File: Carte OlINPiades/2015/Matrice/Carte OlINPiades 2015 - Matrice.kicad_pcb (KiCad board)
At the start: 2 copper layers, 284 parts, among them U1 dsPIC33FJ128MC802, U2 LM7805, U3 LM2937-3.3

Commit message: avancé matrice
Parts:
- removed Batteries1: CONN_2, Connect:bornier2
- removed C1, C5, C6: 100nF, Capacitors_SMD:C_0805_HandSoldering
- removed C2, C7: 10uF, Capacitors_SMD:C_0805_HandSoldering
- removed C4: 330nF, Capacitors_SMD:C_0805_HandSoldering
- removed C8, C9: 0,1uF, Capacitors_SMD:C_0805_HandSoldering
- removed DEMUX1: 74HC4514, Housings_SOIC:SOIC-24_7.5x15.4mm_Pitch1.27mm
- removed Pickit1: CONN_5, Pin_Headers:Pin_Header_Straight_1x05
- removed R1: 10kOhm, Resistors_SMD:R_0805_HandSoldering
- removed R2: 470Ohm, Resistors_SMD:R_0805_HandSoldering
- removed R3: TODO, Resistors_SMD:R_0805_HandSoldering
- removed S1: CAT4016, Housings_SOIC:SOIC-24_7.5x15.4mm_Pitch1.27mm
- removed S2, S3, S4, S5, S6, S7, S8, S9: TPS2080, Housings_SOIC:SOIC-8_3.9x4.9mm_Pitch1.27mm
- removed U1: dsPIC33FJ128MC802, Housings_SOIC:SOIC-28_7.5x17.9mm_Pitch1.27mm
- removed U2: LM7805, Transistors_SMD:sot428
- removed U3: LM2937-3.3, Transistors_SMD:sot428
- removed UART1, UART2: CONN_2, Pin_Headers:Pin_Header_Straight_1x02
- added H1: PinHeader, Pin_Headers:Pin_Header_Straight_1x16, F.Cu at (118.7, 29.9)
- added H2: PinHeader, Pin_Headers:Pin_Header_Straight_1x16, F.Cu at (217.7, 120.5)
- moved D241 43.0 mm to (17.5, 192.3)
- moved D242 40.6 mm to (27.5, 192.3)
- moved D225 40.5 mm to (17.5, 182.3)
- moved D243 38.4 mm to (37.5, 192.3)
- moved D209 38.3 mm to (17.5, 172.3)
- moved D256 38.1 mm to (167.5, 192.3)
- moved D226 38.0 mm to (27.5, 182.3)
- moved D1 37.0 mm to (17.5, 42.3)
- moved D244 36.4 mm to (47.5, 192.3)
- moved D193 36.2 mm to (17.5, 162.3)
- moved D255 36.2 mm to (157.5, 192.3)
- moved D227 35.7 mm to (37.5, 182.3)
- moved D210 35.6 mm to (27.5, 172.3)
- moved D240 35.4 mm to (167.5, 182.3)
- moved D17 35.1 mm to (17.5, 52.3)
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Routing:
- net GND: track 377.5 -> 0.00 mm, vias 8 -> 0
- net +3.3V: track 188.5 -> 0.00 mm, vias 3 -> 0
- net Net-(D1-Pad2): track 148.0 -> 330.0 mm
- net +5V: track 155.1 -> 0.00 mm, vias 8 -> 0
- net RB11: track 101.4 -> 0.00 mm
- net RB10: track 95.8 -> 0.00 mm
- net RB7: track 90.8 -> 0.00 mm, vias 2 -> 0
- net RB6: track 87.1 -> 0.00 mm, vias 2 -> 0
- net RB9: track 86.4 -> 0.00 mm
- net RB8: track 82.2 -> 0.00 mm
- net RA2: track 69.2 -> 0.00 mm
- net RB3: track 67.0 -> 0.00 mm
- net RB2: track 66.5 -> 0.00 mm
- net Net-(DEMUX1-Pad16): track 64.6 -> 0.00 mm
- net Net-(DEMUX1-Pad15): track 63.6 -> 0.00 mm
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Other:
- rule trace_min: 0.2 -> 0.25

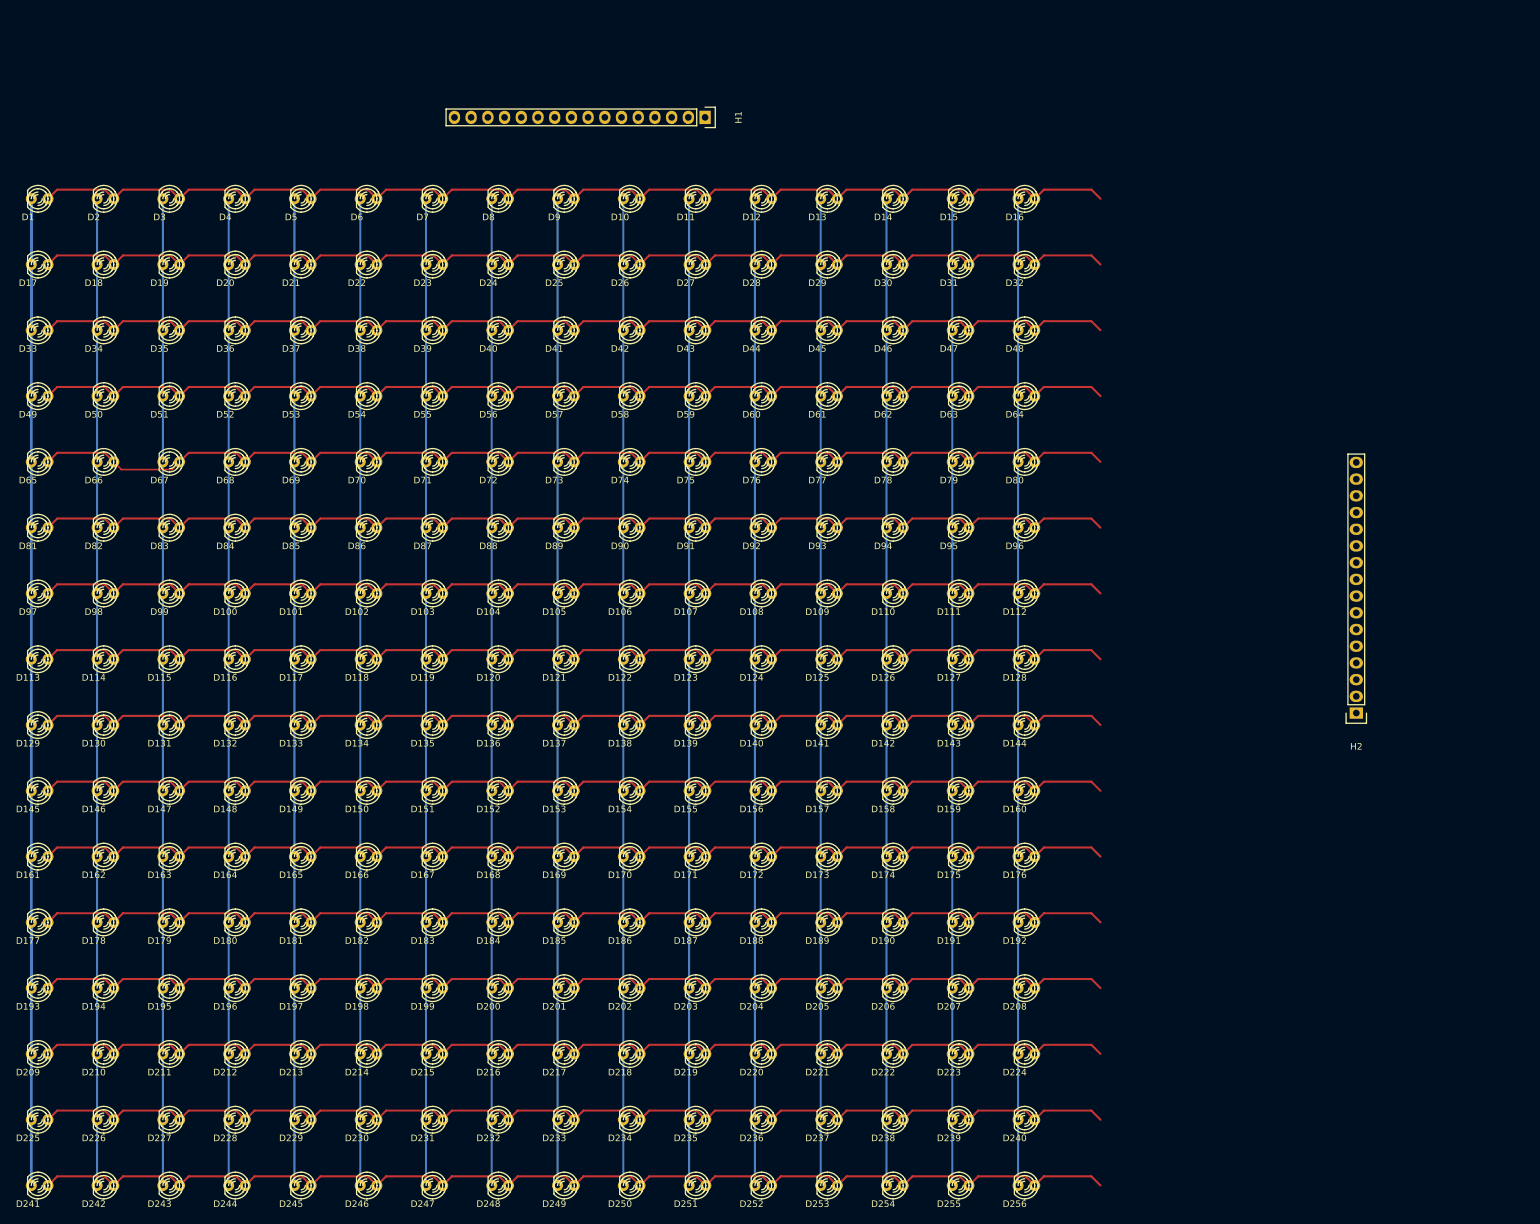
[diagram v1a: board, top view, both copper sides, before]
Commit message: fini plaque de leds
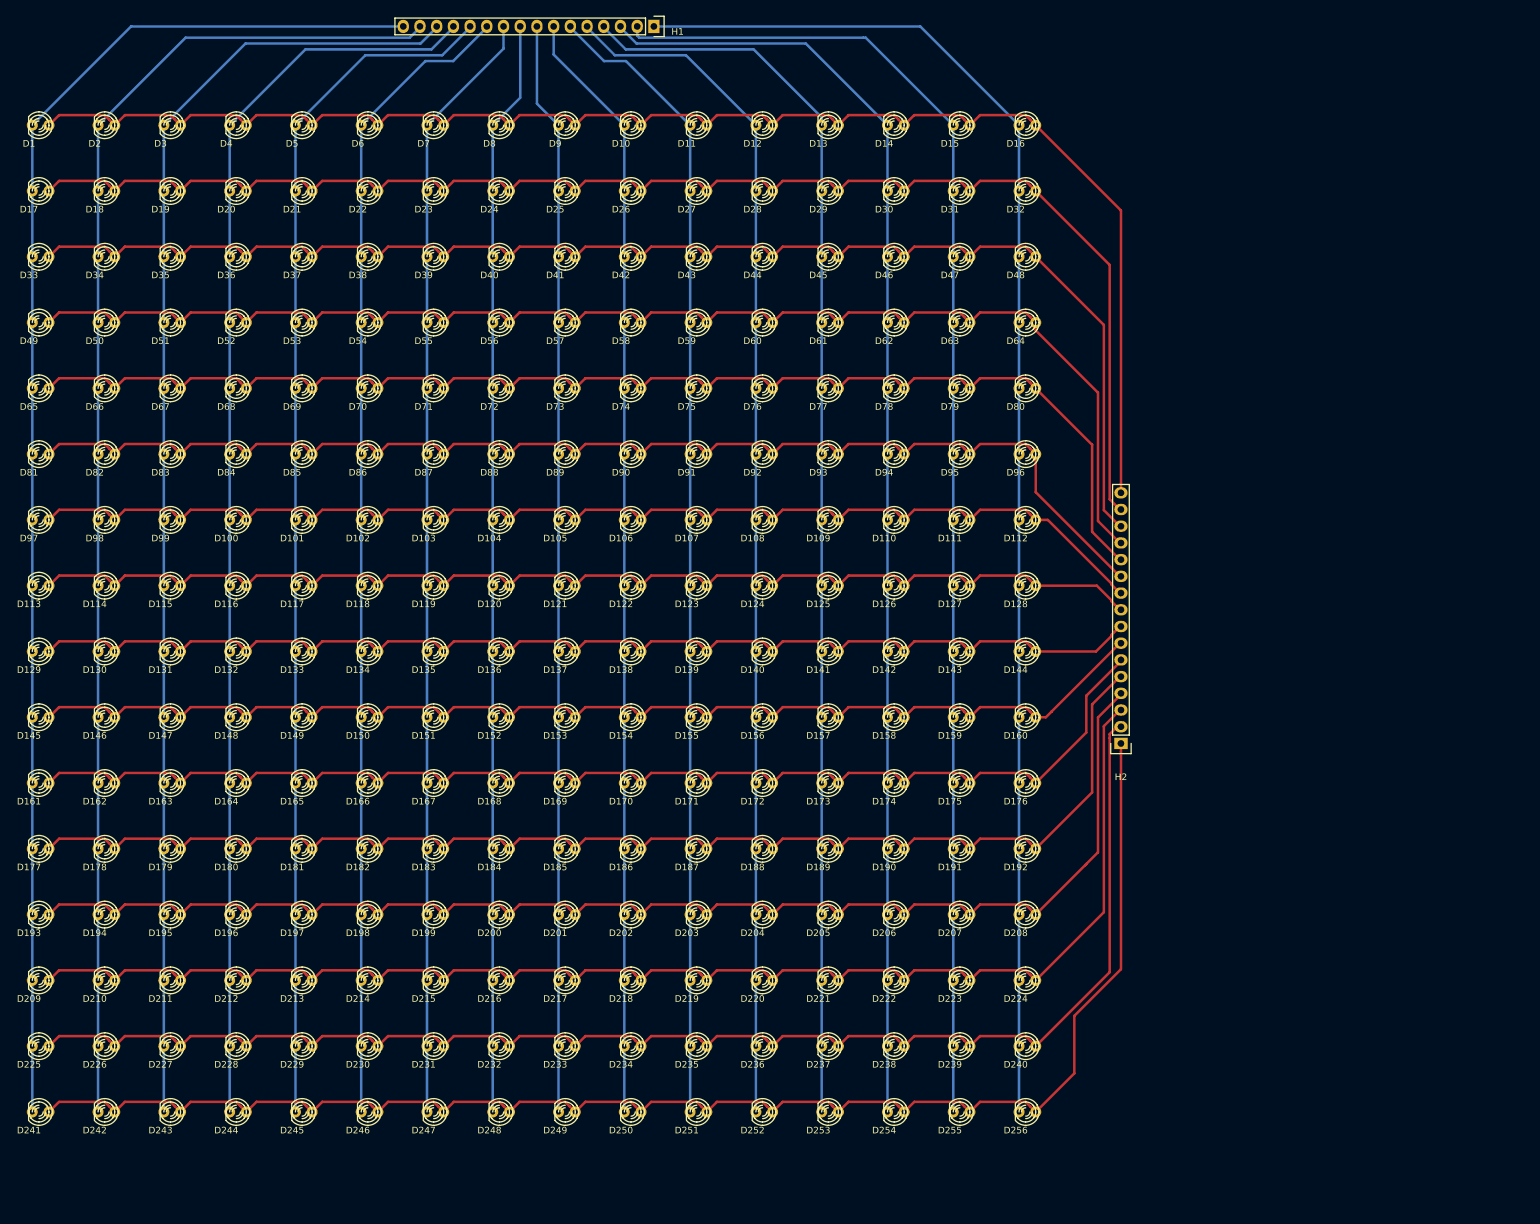
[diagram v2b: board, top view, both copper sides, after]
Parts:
- moved H2 36.1 mm to (181.9, 125.1)
- moved H1 15.9 mm to (110.9, 16.1)
- moved D1 11.2 mm to (17.7, 31.1)
- moved D10 11.2 mm to (107.7, 31.1)
- moved D100 11.2 mm to (47.7, 91.1)
- moved D101 11.2 mm to (57.7, 91.1)
- moved D102 11.2 mm to (67.7, 91.1)
- moved D103 11.2 mm to (77.7, 91.1)
- moved D104 11.2 mm to (87.7, 91.1)
- moved D105 11.2 mm to (97.7, 91.1)
- moved D106 11.2 mm to (107.7, 91.1)
- moved D107 11.2 mm to (117.7, 91.1)
- moved D108 11.2 mm to (127.7, 91.1)
- moved D109 11.2 mm to (137.7, 91.1)
- moved D11 11.2 mm to (117.7, 31.1)
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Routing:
- net Net-(D1-Pad2): track 330.0 -> 212.6 mm
- net Net-(D112-Pad2): track 150.0 -> 211.7 mm
- net Net-(D241-Pad1): track 178.5 -> 234.2 mm
- net Net-(D1-Pad1): track 178.5 -> 234.1 mm
- net Net-(D111-Pad2): track 150.0 -> 205.1 mm
- net Net-(D225-Pad1): track 178.5 -> 227.1 mm
- net Net-(D17-Pad1): track 178.5 -> 226.7 mm
- net Net-(D115-Pad2): track 150.0 -> 197.8 mm
- net Net-(D110-Pad2): track 150.0 -> 196.9 mm
- net Net-(D209-Pad1): track 178.5 -> 219.4 mm
- net Net-(D33-Pad1): track 178.5 -> 219.2 mm
- net Net-(D100-Pad2): track 150.0 -> 190.3 mm
- net Net-(D109-Pad2): track 150.0 -> 190.1 mm
- net Net-(D193-Pad1): track 178.5 -> 212.2 mm
- net Net-(D49-Pad1): track 178.5 -> 211.8 mm
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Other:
- net class Default: clearance 0.2 -> 0.4; trace_width 0.25 -> 0.308; via_dia 0.6 -> 0.8; via_drill 0.4 -> 0.6
- net class Pisa interm added: clearance 0.508, trace_width 0.381, via_dia 1, via_drill 0.8
- rule trace_clearance: 0.2 -> 0.4
- rule trace_min: 0.25 -> 0.308

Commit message: retourné matrice, exporté pdfs
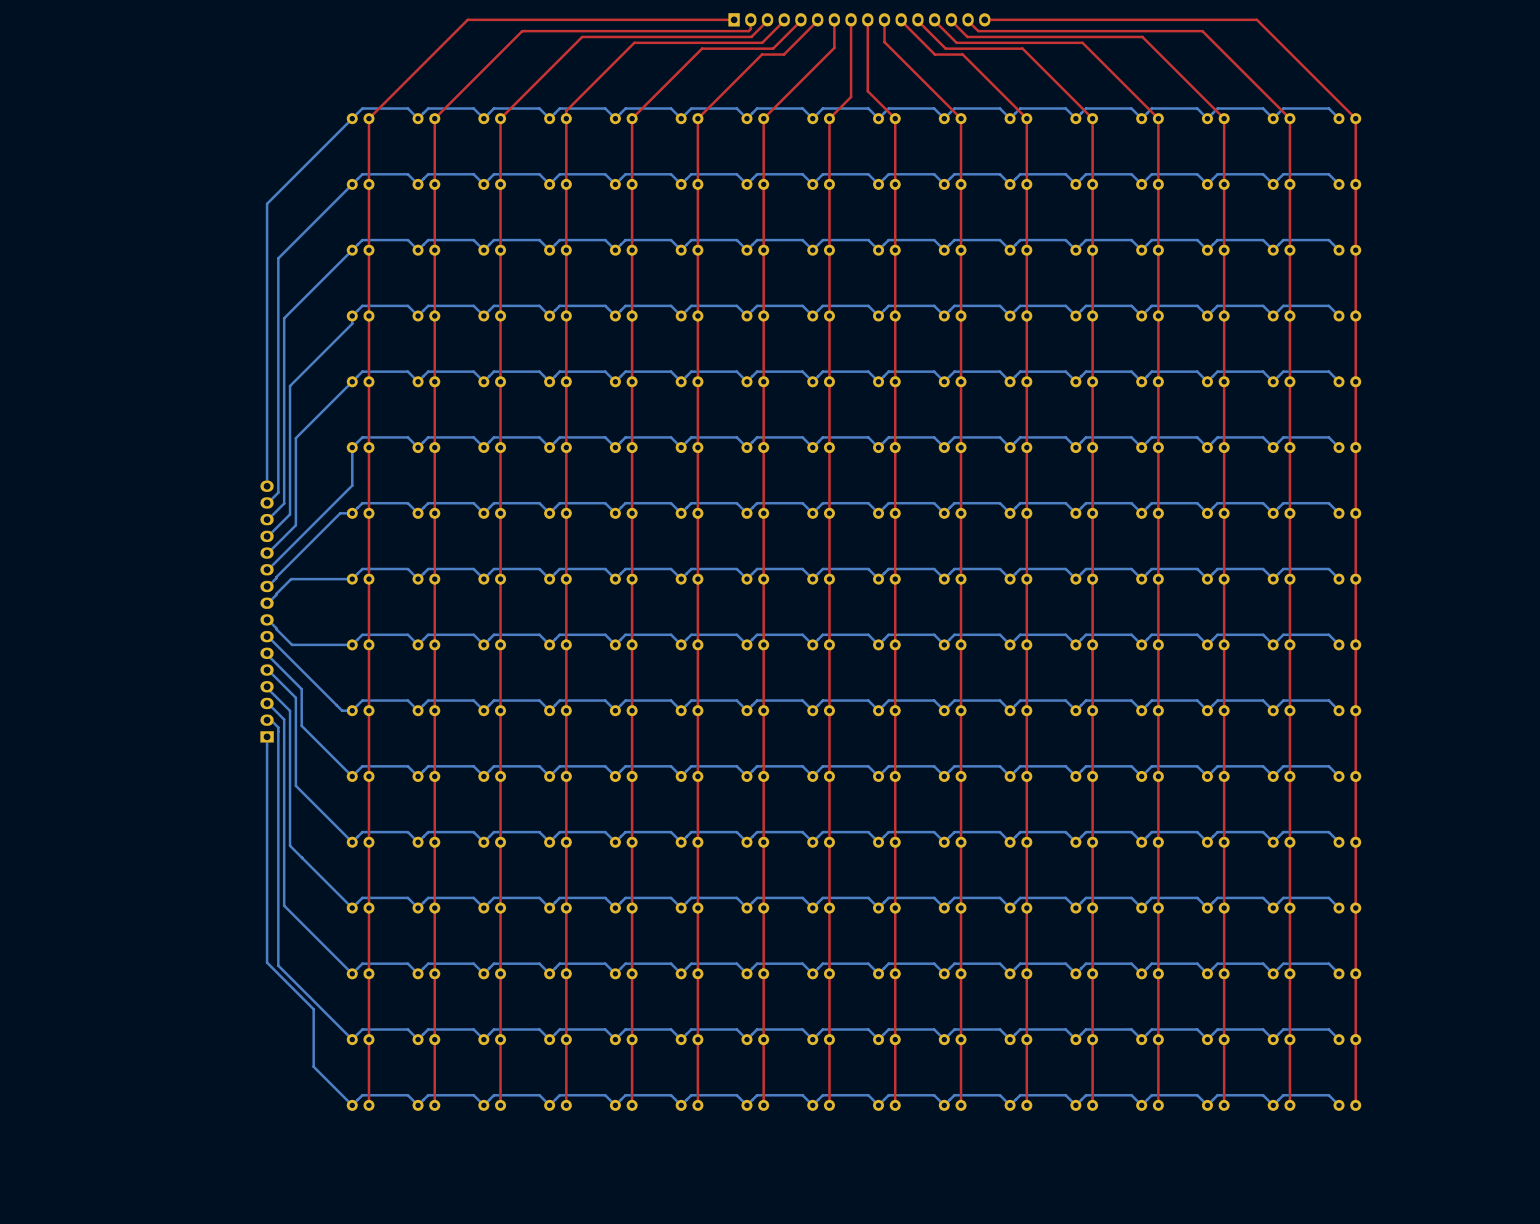
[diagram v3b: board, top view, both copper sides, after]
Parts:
- D1, D10, D100, D101, D102, D103, D104, D105, D106, D107, D108, D109, D11, D110, D111, D112, D113, D114, D115, D116, D117, D118, D119, D12, D120, D121, D122, D123, D124, D125, D126, D127, D128, D129, D13, D130, D131, D132, D133, D134, D135, D136, D137, D138, D139, D14, D140, D141, D142, D143, D144, D145, D146, D147, D148, D149, D15, D150, D151, D152, D153, D154, D155, D156, D157, D158, D159, D16, D160, D161, D162, D163, D164, D165, D166, D167, D168, D169, D17, D170, D171, D172, D173, D174, D175, D176, D177, D178, D179, D18, D180, D181, D182, D183, D184, D185, D186, D187, D188, D189, D19, D190, D191, D192, D193, D194, D195, D196, D197, D198, D199, D2, D20, D200, D201, D202, D203, D204, D205, D206, D207, D208, D209, D21, D210, D211, D212, D213, D214, D215, D216, D217, D218, D219, D22, D220, D221, D222, D223, D224, D225, D226, D227, D228, D229, D23, D230, D231, D232, D233, D234, D235, D236, D237, D238, D239, D24, D240, D241, D242, D243, D244, D245, D246, D247, D248, D249, D25, D250, D251, D252, D253, D254, D255, D256, D26, D27, D28, D29, D3, D30, D31, D32, D33, D34, D35, D36, D37, D38, D39, D4, D40, D41, D42, D43, D44, D45, D46, D47, D48, D49, D5, D50, D51, D52, D53, D54, D55, D56, D57, D58, D59, D6, D60, D61, D62, D63, D64, D65, D66, D67, D68, D69, D7, D70, D71, D72, D73, D74, D75, D76, D77, D78, D79, D8, D80, D81, D82, D83, D84, D85, D86, D87, D88, D89, D9, D90, D91, D92, D93, D94, D95, D96, D97, D98, D99, H1, H2: moved to B.Cu
- moved D1 198.6 mm to (216.3, 30.1), turned to 0 degrees
- moved D113 198.6 mm to (216.3, 100.1), turned to 0 degrees
- moved D129 198.6 mm to (216.3, 110.1), turned to 0 degrees
- moved D145 198.6 mm to (216.3, 120.1), turned to 0 degrees
- moved D161 198.6 mm to (216.3, 130.1), turned to 0 degrees
- moved D17 198.6 mm to (216.3, 40.1), turned to 0 degrees
- moved D177 198.6 mm to (216.3, 140.1), turned to 0 degrees
- moved D193 198.6 mm to (216.3, 150.1), turned to 0 degrees
- moved D209 198.6 mm to (216.3, 160.1), turned to 0 degrees
- moved D225 198.6 mm to (216.3, 170.1), turned to 0 degrees
- moved D241 198.6 mm to (216.3, 180.1), turned to 0 degrees
- moved D33 198.6 mm to (216.3, 50.1), turned to 0 degrees
- moved D49 198.6 mm to (216.3, 60.1), turned to 0 degrees
- moved D65 198.6 mm to (216.3, 70.1), turned to 0 degrees
- moved D81 198.6 mm to (216.3, 80.1), turned to 0 degrees
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
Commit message: change coté des pistes des broches de la matrice de leds
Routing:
- net Net-(D209-Pad1): track 219.4 -> 231.4 mm
- net Net-(D225-Pad1): track 227.1 -> 228.2 mm
